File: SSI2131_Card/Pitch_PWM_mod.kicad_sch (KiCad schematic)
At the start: 42 parts, among them Q1 2N3906, Q2 2N3906, U1 CD4066BM, U2 OPA1678, U3 OPA1678, U4 LM13700, U8 OPA1678

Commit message: Added pin lables and added VCOs into their own heiarchy sheets
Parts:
- added C20, C21: 0.1uf, Capacitor_SMD:C_0603_1608Metric, symbol Device:C
- U8: footprint (none) -> Package_SO:SOIC-8_3.9x4.9mm_P1.27mm
- renumbered C1 to C10, C19 to C11, C13 to C12, C15 to C13, C17 to C14, C14 to C15, C18 to C17, C6 to C18, C3 to C19, C5 to C9, R3 to R15, R8 to R16, R19 to R18, R2 to R19, R7 to R20, R10 to R21, R14 to R22, R6 to R23, R12 to R24, R32 to R25, R18 to R26, R35 to R27, R33 to R28, R21 to R29, R4 to R30, R9 to R31, R34 to R32, R31 to R33, R13 to R34, R15 to R35, TP1 to TP2, U2 to U5, U1 to U6, U3 to U7
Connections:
- net +5V: now also U8.8 (V+), C20.1
- net -12V: now also U8.4 (V-), C21.1
- net GND: now also C20.2, C21.2
- net PMOD_B_AMT renamed PWM_MOD_AMOUNT
- net PMOD_B_EN renamed PWM_MOD_EN
- net PMOD_B_IN renamed PWM_MOD_IN
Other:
- moved on the sheet: U6C, U6D, U8C

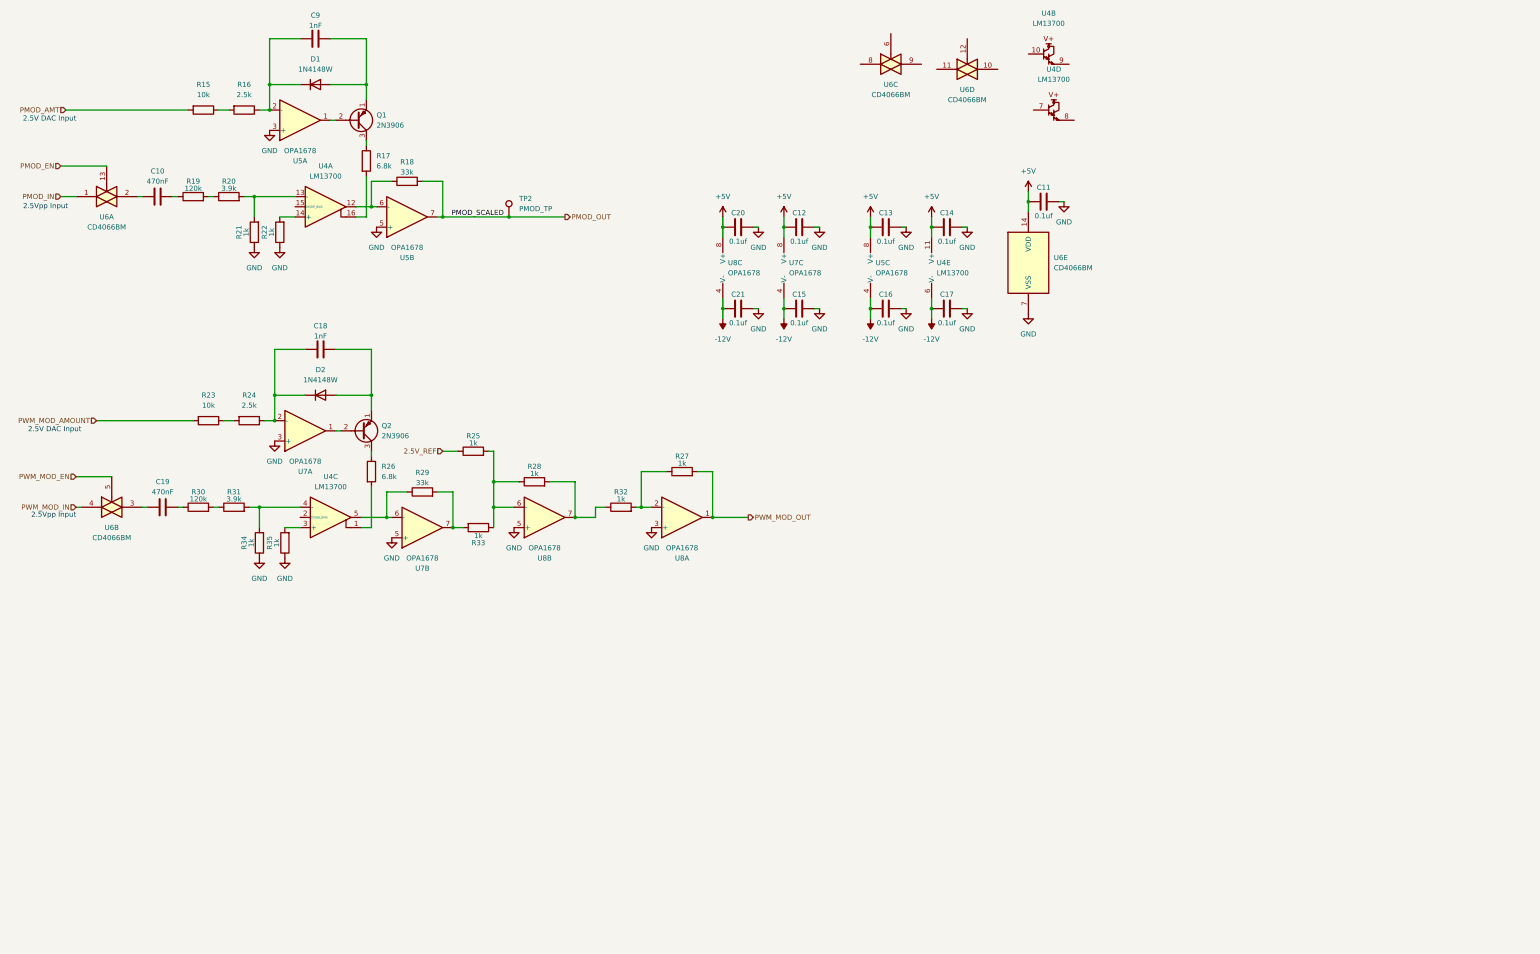
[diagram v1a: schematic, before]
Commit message: Added Biasing for CD4066 switches. Added biasing pot for PWM mod.
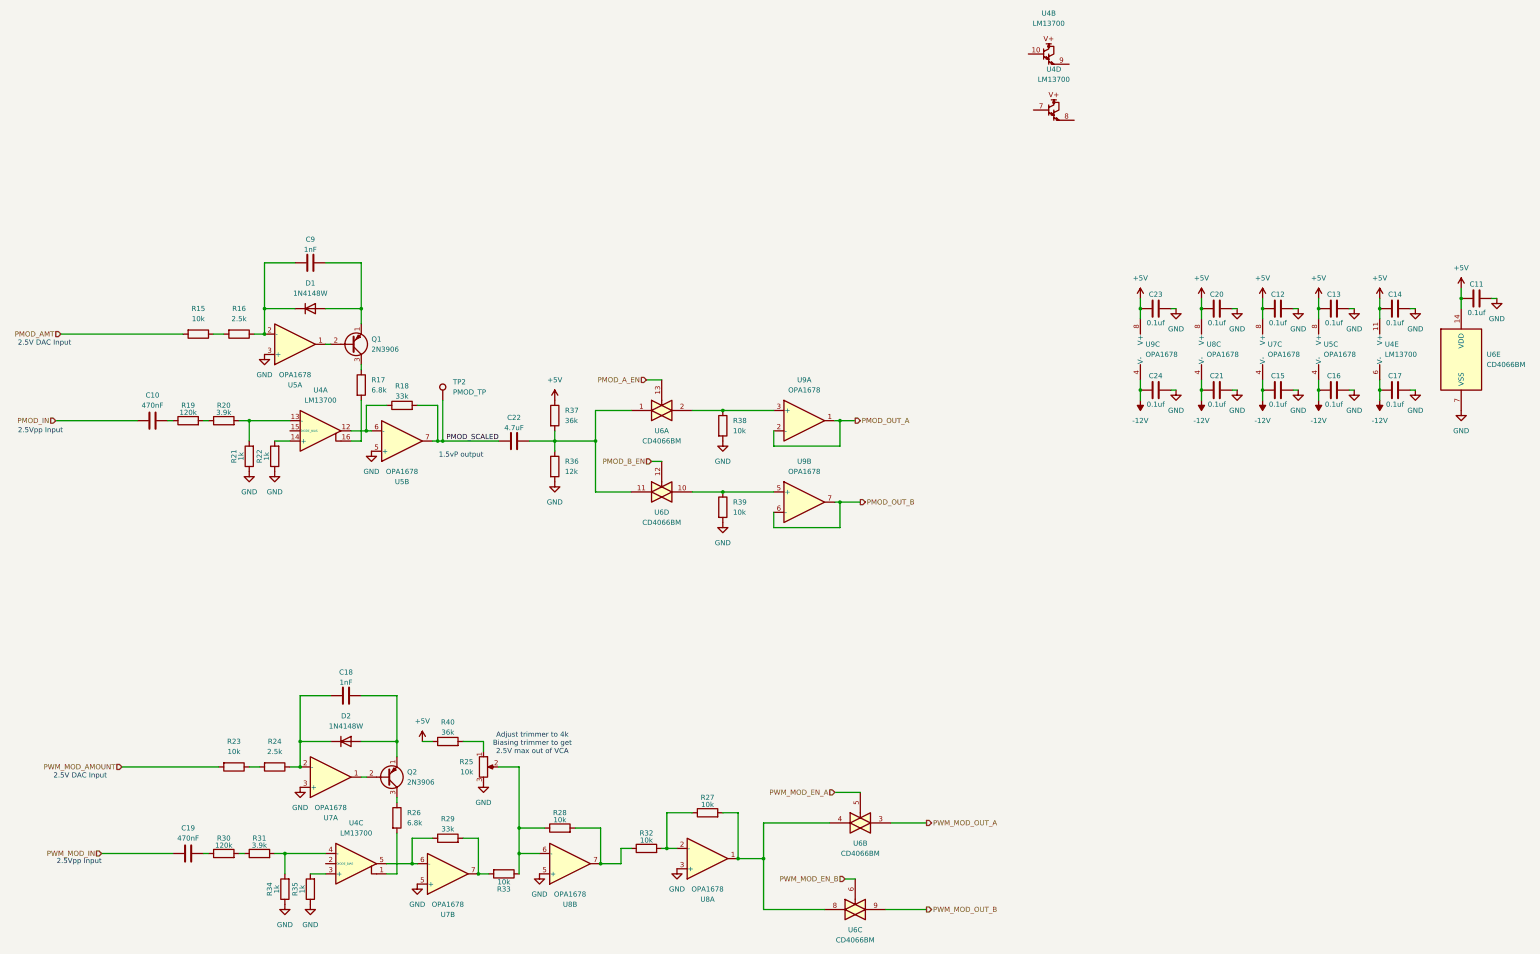
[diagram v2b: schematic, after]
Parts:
- removed R25: 1k, Resistor_SMD:R_0603_1608Metric, symbol Device:R
- added C22: 4.7uF, Capacitor_SMD:C_0603_1608Metric, symbol Device:C
- added C23, C24: 0.1uf, Capacitor_SMD:C_0603_1608Metric, symbol Device:C
- added R25: 10k, Potentiometer_THT:Potentiometer_Bourns_3296W_Vertical, symbol Device:R_Potentiometer
- added R36: 12k, Resistor_SMD:R_0603_1608Metric, symbol Device:R
- added R37, R40: 36k, Resistor_SMD:R_0603_1608Metric, symbol Device:R
- added R38, R39: 10k, Resistor_SMD:R_0603_1608Metric, symbol Device:R
- added U9: OPA1678, symbol Amplifier_Operational:OPA1678
- R27, R28, R32, R33: value 1k -> 10k
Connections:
- net PWM_MOD_OUT is gone; now on an unnamed net: R27.2, U8.1
- net +5V: now also C23.1, R37.1, R40.1, U9.8 (V+)
- net -12V: now also C24.1, U9.4 (V-)
- net GND: now also C23.2, C24.2, R25.3, R36.2, R38.2, R39.2
- net PMOD_IN: now also C10.1; no longer U6.1
- net PWM_MOD_IN: now also C19.1; no longer U6.4
- net PWM_MOD_OUT_A: now reaches U6.3
- net PWM_MOD_OUT_A: no longer C19.1
- net at R28.1, R33.1, U8.6 (-): now also R25.2
- net at U6.10: now also R39.1, U9.5 (+)
- net at U6.11: now also U6.1, C22.2, R36.1, R37.2
- net PMOD_B_EN: now reaches U6.12
- net at U6.2: now also R38.1, U9.3 (+); no longer C10.1
- net PWM_MOD_EN_B: now reaches U6.6
- net at U6.8: now also U6.4
- net PWM_MOD_OUT_B: now reaches U6.9
- net PMOD_EN renamed PMOD_A_EN
- net PMOD_OUT renamed PMOD_SCALED
- net PMOD_SCALED: now also C22.1
- net PWM_MOD_EN renamed PWM_MOD_EN_A
- new net: R25.1, R40.2
- new net PMOD_OUT_A: U9.1, U9.2 (-)
- new net PMOD_OUT_B: U9.6 (-), U9.7
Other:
- note added: "1.5vP output"
- note added: "Adjust trimmer to 4k Biasing trimmer to get 2.5V max out of VCA"
- moved on the sheet: C10, C11, C12, C13, C14, C15, C16, C17, C18, C19, C20, C21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

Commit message: added connections for lfo adn pmod
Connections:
- net PWM_MOD_EN_B is gone; now on net PWM_MOD_EN_A: U6.6
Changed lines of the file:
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@@
 		)
 	)
-	(hierarchical_label "PWM_MOD_EN_B"
+	(hierarchical_label "PWM_MOD_EN_A"
 		(shape input)
 		(at 226.06 234.95 180)
